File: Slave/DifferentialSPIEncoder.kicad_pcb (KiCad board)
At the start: 2 copper layers, 52.3 x 42.7 mm, 31 parts, among them J1 Debug, J2 8P8C_LED_Shielded, U2 AS5048A, U3 SN65HVD06D, U4 SN65HVD06D, U5 SN65HVD06D

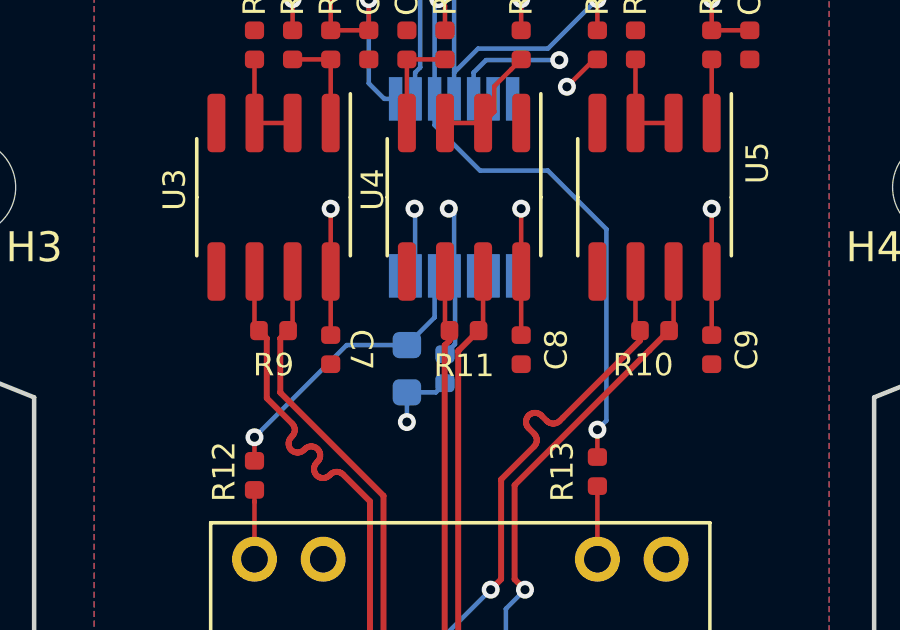
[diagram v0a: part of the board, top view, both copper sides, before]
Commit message: Swap AS5048A with AS5047U
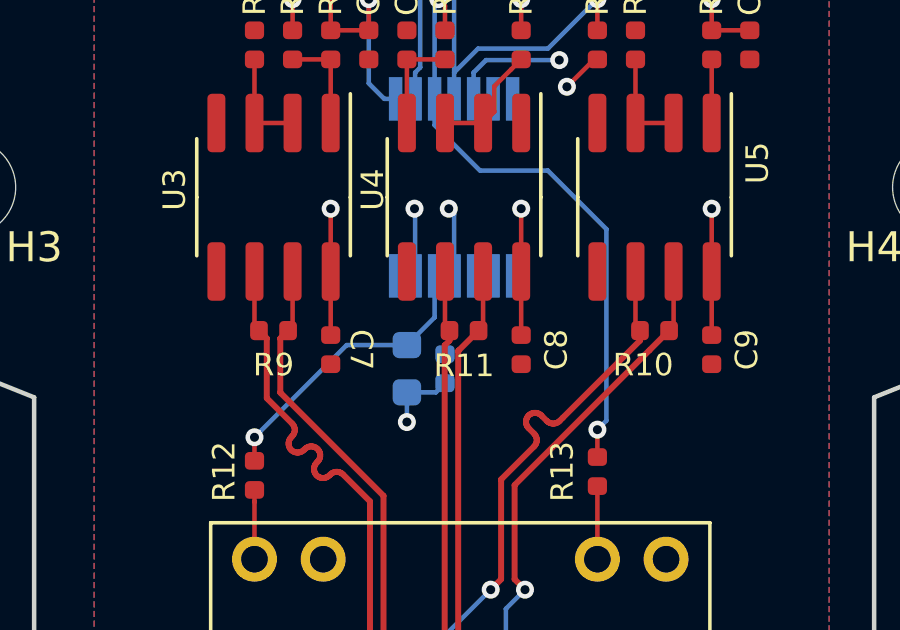
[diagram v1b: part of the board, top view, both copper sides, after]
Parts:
- removed C3: 100nF, Capacitor_SMD:C_0402_1005Metric
- removed U2: AS5048A, Package_SO:TSSOP-14_4.4x5mm_P0.65mm
- added C2: 1uF, Capacitor_SMD:C_0603_1608Metric, B.Cu at (98.4, 106.0)
- added U1: AS5047U, Package_SO:TSSOP-14_4.4x5mm_P0.65mm, B.Cu at (100.0, 100.0)
- C1: value 10uF -> 100nF; footprint Capacitor_SMD:C_0603_1608Metric -> Capacitor_SMD:C_0402_1005Metric
- moved C1 1.27 mm to (99.7, 106.0)
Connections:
- C1 pad 1: V3cap -> +5V
- R12 pad 2: V3cap -> +3V3
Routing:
- net V3cap: track 9.83 -> 0.00 mm, vias 1 -> 0
- net +3V3: track 0.00 -> 9.83 mm, vias 0 -> 1
- net +5V: track 21.2 -> 18.4 mm

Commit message: Update PCB
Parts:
- removed R1: 1k, Resistor_SMD:R_0402_1005Metric
- removed U5: SN65HVD06D, Package_SO:SOIC-8_3.9x4.9mm_P1.27mm
- added U2: MAX14783ExS, Package_SO:SOIC-8_3.9x4.9mm_P1.27mm, F.Cu at (94.0, 100.3)
- U3, U4: value SN65HVD06D -> MAX14783ExS
- moved U4 6.35 mm to (106.7, 100.3)
- moved U3 6.35 mm to (100.3, 100.3)
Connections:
- U3 pad 1: Net-(R2-Pad1) -> Net-(U3-Pad1)
- U3 pad 2: Net-(R7-Pad1) -> Net-(R8-Pad2)
- U3 pad 3: Net-(R7-Pad1) -> Net-(R8-Pad2)
- U3 pad 4: Net-(U3-Pad4) -> Net-(C6-Pad1)
- U3 pad 6: /CS_+ -> /MISO_+
- U3 pad 7: /CS_- -> /MISO_-
- U4 pad 1: Net-(U4-Pad1) -> Net-(R3-Pad1)
- U4 pad 2: Net-(R8-Pad2) -> Net-(R5-Pad1)
- U4 pad 3: Net-(R8-Pad2) -> Net-(R5-Pad1)
- U4 pad 4: Net-(C6-Pad1) -> Net-(U4-Pad4)
- U4 pad 6: /MISO_+ -> /CLK_+
- U4 pad 7: /MISO_- -> /CLK_-

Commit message: Fix Slave
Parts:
- removed J2: 8P8C_LED_Shielded, Connector_RJ:RJ45_Amphenol_RJHSE538X
- removed R12, R13: 220, Resistor_SMD:R_0402_1005Metric
- added C3: 1uF, Capacitor_SMD:C_0603_1608Metric_Pad1.05x0.95mm_HandSolder, F.Cu at (123.9, 79.5)
- added R1: 1k, Resistor_SMD:R_0603_1608Metric_Pad1.05x0.95mm_HandSolder, F.Cu at (115.2, 79.5)
- added U5: MA702, Package_DFN_QFN:QFN-16-1EP_3x3mm_P0.5mm_EP1.8x1.8mm, F.Cu at (107.2, 84.8)
- C1, C7, C8, C9: footprint Capacitor_SMD:C_0402_1005Metric -> Capacitor_SMD:C_0603_1608Metric_Pad1.05x0.95mm_HandSolder
- C2: footprint Capacitor_SMD:C_0603_1608Metric -> Capacitor_SMD:C_0603_1608Metric_Pad1.05x0.95mm_HandSolder
- C4, C5: value 2.2pF -> C; footprint Capacitor_SMD:C_0402_1005Metric -> Capacitor_SMD:C_0603_1608Metric_Pad1.05x0.95mm_HandSolder
- C6: value 2.2pF -> 22nF; footprint Capacitor_SMD:C_0402_1005Metric -> Capacitor_SMD:C_0603_1608Metric_Pad1.05x0.95mm_HandSolder
- J1: value Debug -> RJ45_Shielded; footprint Connector_PinHeader_2.54mm:PinHeader_2x03_P2.54mm_Vertical -> Connector_RJ:RJ45_Amphenol_RJHSE5380
- R10, R11, R2, R8: footprint Resistor_SMD:R_0402_1005Metric -> Resistor_SMD:R_0603_1608Metric_Pad1.05x0.95mm_HandSolder
- R3, R4: value 1k -> 10k; footprint Resistor_SMD:R_0402_1005Metric -> Resistor_SMD:R_0603_1608Metric_Pad1.05x0.95mm_HandSolder
- R5: value 10k -> 120; footprint Resistor_SMD:R_0402_1005Metric -> Resistor_SMD:R_0603_1608Metric_Pad1.05x0.95mm_HandSolder
- R6, R7: value 10k -> 1k; footprint Resistor_SMD:R_0402_1005Metric -> Resistor_SMD:R_0603_1608Metric_Pad1.05x0.95mm_HandSolder
- R9: value 120 -> 10k; footprint Resistor_SMD:R_0402_1005Metric -> Resistor_SMD:R_0603_1608Metric_Pad1.05x0.95mm_HandSolder
- U1: value AS5047U -> AS5048A
- moved R9 35.0 mm to (115.2, 77.0), turned to 0 degrees
- moved C9 32.3 mm to (123.9, 77.0), turned to 0 degrees
- moved C8 31.2 mm to (119.5, 79.5), turned to 0 degrees
- moved R2 23.1 mm to (116.3, 84.5), turned to 0 degrees
- moved R10 22.0 mm to (112.0, 83.4), turned to 0 degrees
- moved U4 21.5 mm to (108.8, 78.9), turned to 0 degrees
- moved R4 21.3 mm to (116.3, 82.0), turned to 0 degrees
- moved C5 20.7 mm to (119.5, 77.0), turned to 0 degrees
- moved C6 16.5 mm to (112.0, 85.9), turned to 0 degrees
- moved R8 16.3 mm to (116.3, 87.0), turned to 0 degrees
- moved R7 14.9 mm to (106.7, 88.7), turned to 0 degrees
- moved R11 13.1 mm to (107.4, 93.7), turned to 0 degrees
- moved J1 12.9 mm to (90.7, 84.7), turned to 0 degrees
- moved C7 12.8 mm to (103.0, 94.8), turned to 0 degrees
- moved R6 12.8 mm to (106.7, 91.2), turned to 0 degrees
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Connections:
- C4 pad 1: ~CSn -> /~CSn
- C5 pad 1: CLK -> /CLK
- J1 pad 1: MISO -> GNDD
- J1 pad 3: CLK -> /CLK-
- J1 pad 4: /MOSI -> /MISO-
- J1 pad 5: ~CSn -> /MISO+
- J1 pad 6: GND -> /CLK+
- R10 pad 1: /CLK_- -> /MISO+
- R10 pad 2: /CLK_+ -> /MISO-
- R11 pad 1: /MISO_- -> /CLK+
- R11 pad 2: /MISO_+ -> /CLK-
- R2 pad 2: ~CSn -> /~CSn
- R3 pad 1: Net-(R3-Pad1) -> Net-(R2-Pad1)
- R3 pad 2: CLK -> +5V
- R4 pad 1: MISO -> GND
- R4 pad 2: Net-(C6-Pad1) -> Net-(R4-Pad2)
- R5 pad 1: Net-(R5-Pad1) -> /CS+
- R5 pad 2: GND -> /CS-
- R6 pad 1: +5V -> /MISO
- R6 pad 2: Net-(R2-Pad1) -> Net-(C6-Pad1)
- R7 pad 2: GND -> /CLK
- R8 pad 1: +5V -> Net-(R8-Pad1)
- R8 pad 2: Net-(R8-Pad2) -> +5V
- R9 pad 1: /CS_- -> GND
- R9 pad 2: /CS_+ -> Net-(R9-Pad2)
- U1 pad 1: ~CSn -> (no net)
- U1 pad 10: Net-(U1-Pad10) -> (no net)
- U1 pad 14: /I -> (no net)
- U1 pad 2: CLK -> (no net)
- U1 pad 3: MISO -> (no net)
- U1 pad 4: /MOSI -> (no net)
- U1 pad 6: /B -> (no net)
- U1 pad 7: /A -> (no net)
- U1 pad 8: Net-(U1-Pad8) -> (no net)
- U1 pad 9: Net-(U1-Pad9) -> (no net)
- U2 pad 2: Net-(R7-Pad1) -> Net-(R4-Pad2)
- U2 pad 3: Net-(R7-Pad1) -> Net-(R4-Pad2)
- U2 pad 6: /CS_+ -> /CS+
- U2 pad 7: /CS_- -> /CS-
- U3 pad 2: Net-(R8-Pad2) -> Net-(R8-Pad1)
- U3 pad 3: Net-(R8-Pad2) -> Net-(R8-Pad1)
- U3 pad 6: /MISO_+ -> /MISO+
- U3 pad 7: /MISO_- -> /MISO-
- U4 pad 1: Net-(R3-Pad1) -> Net-(R7-Pad1)
- U4 pad 2: Net-(R5-Pad1) -> Net-(R9-Pad2)
- U4 pad 3: Net-(R5-Pad1) -> Net-(R9-Pad2)
- U4 pad 6: /CLK_+ -> /CLK+
- U4 pad 7: /CLK_- -> /CLK-
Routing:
- net /CLK-: track 0.00 -> 41.1 mm, vias 0 -> 1
- net MISO: track 27.6 -> 0.00 mm, vias 2 -> 0
- net +5V: track 18.4 -> 43.6 mm
- net CLK: track 24.8 -> 0.00 mm, vias 1 -> 0
- net Net-(R8-Pad1): track 0.00 -> 19.4 mm, vias 0 -> 1
- net Net-(R4-Pad2): track 0.00 -> 18.8 mm, vias 0 -> 1
- net /CLK_+: track 18.8 -> 0.00 mm, vias 1 -> 0
- net Net-(R1-Pad2): track 0.00 -> 18.8 mm, vias 0 -> 1
- net /CLK_-: track 18.8 -> 0.00 mm, vias 1 -> 0
- net Net-(J2-PadSH): track 17.8 -> 0.00 mm
- net /MISO: track 0.00 -> 17.8 mm
- net /MISO+: track 0.00 -> 17.8 mm
- net /CS_+: track 17.8 -> 0.00 mm
- net /CS_-: track 17.8 -> 0.00 mm
- net /CS-: track 0.00 -> 17.8 mm
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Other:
- net class Default removed

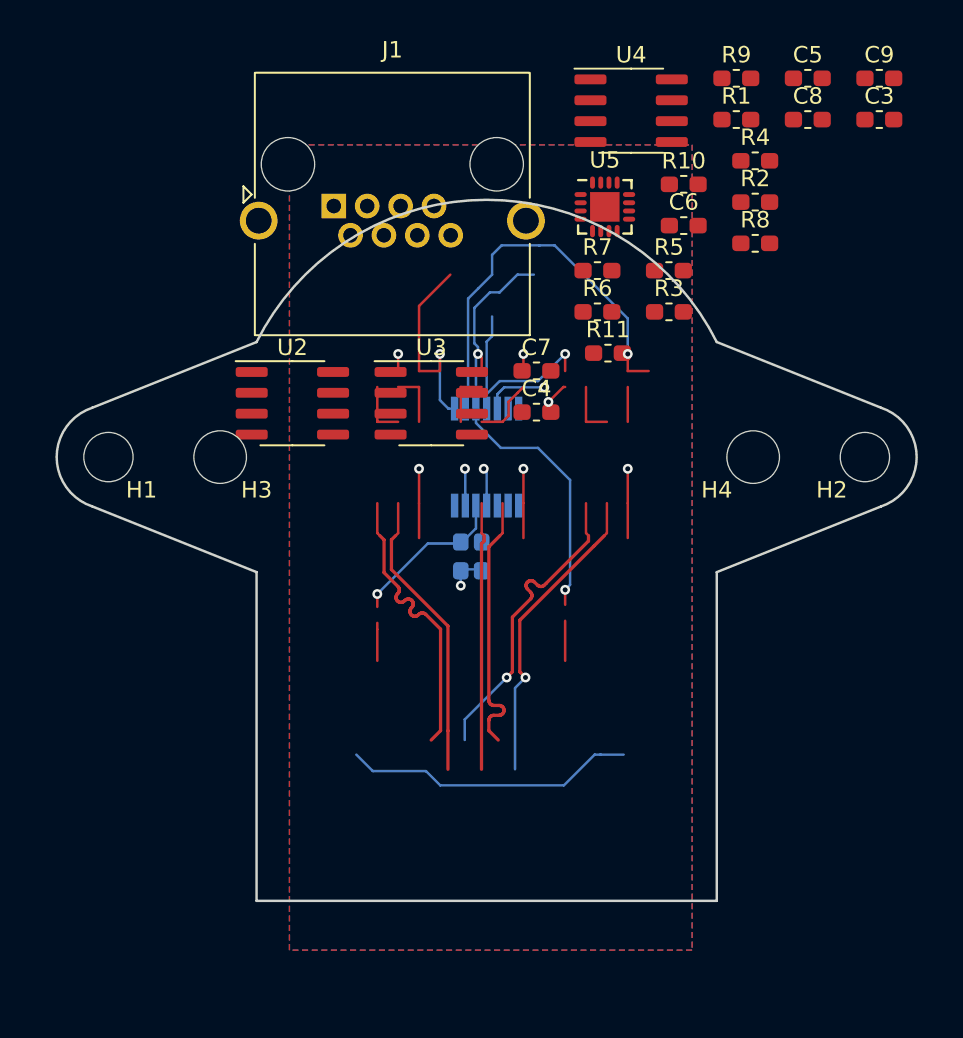
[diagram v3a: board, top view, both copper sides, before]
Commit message: Revert slave pcb to older build of Kicad
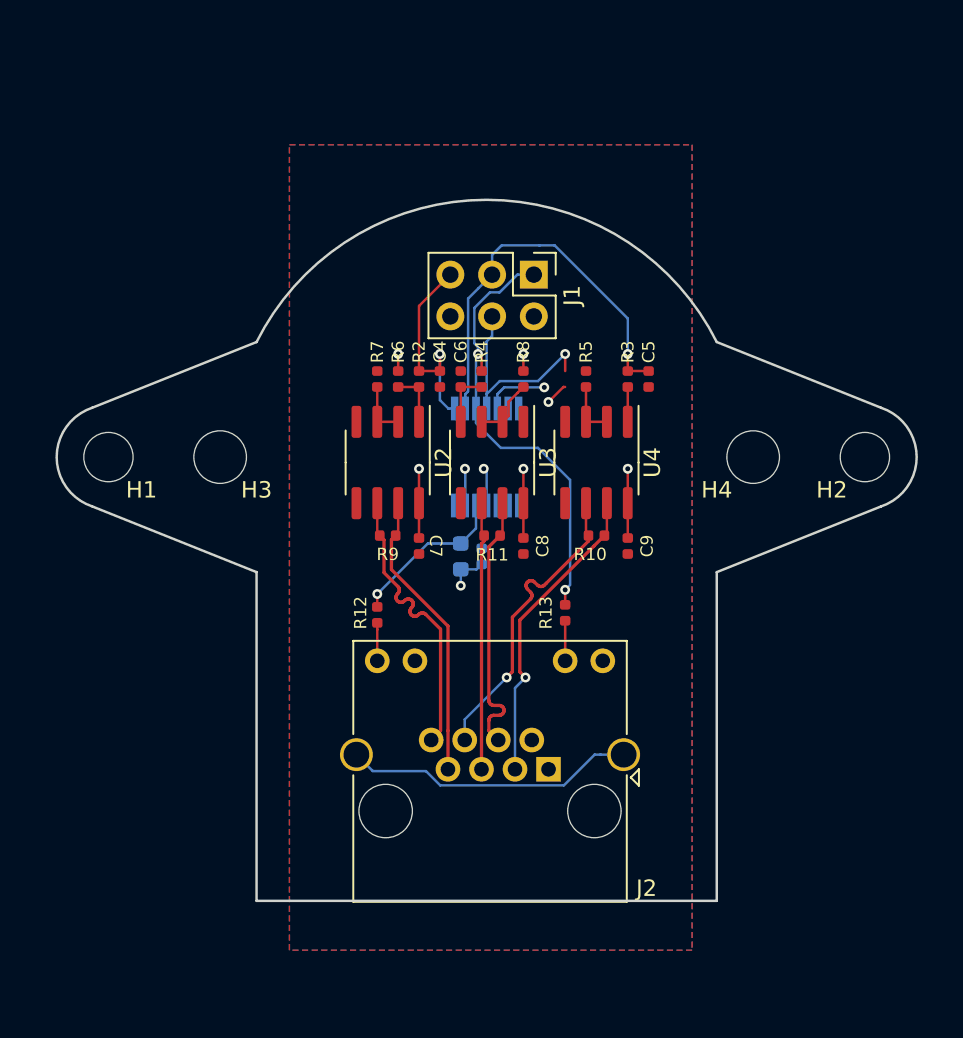
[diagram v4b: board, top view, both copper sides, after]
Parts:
- removed C3: 1uF, Capacitor_SMD:C_0603_1608Metric_Pad1.05x0.95mm_HandSolder
- removed R1: 1k, Resistor_SMD:R_0603_1608Metric_Pad1.05x0.95mm_HandSolder
- removed U5: MA702, Package_DFN_QFN:QFN-16-1EP_3x3mm_P0.5mm_EP1.8x1.8mm
- added J2: 8P8C_LED_Shielded, Connector_RJ:RJ45_Amphenol_RJHSE538X, F.Cu at (103.8, 119.0)
- added R12: 220, Resistor_SMD:R_0402_1005Metric, F.Cu at (93.3, 109.6)
- added R13: 220, Resistor_SMD:R_0402_1005Metric, F.Cu at (104.8, 109.5)
- C1, C7, C8, C9: footprint Capacitor_SMD:C_0603_1608Metric_Pad1.05x0.95mm_HandSolder -> Capacitor_SMD:C_0402_1005Metric
- C2: footprint Capacitor_SMD:C_0603_1608Metric_Pad1.05x0.95mm_HandSolder -> Capacitor_SMD:C_0603_1608Metric
- C4, C5: value C -> 2.2pF; footprint Capacitor_SMD:C_0603_1608Metric_Pad1.05x0.95mm_HandSolder -> Capacitor_SMD:C_0402_1005Metric
- C6: value 22nF -> 2.2pF; footprint Capacitor_SMD:C_0603_1608Metric_Pad1.05x0.95mm_HandSolder -> Capacitor_SMD:C_0402_1005Metric
- J1: value RJ45_Shielded -> Debug; footprint Connector_RJ:RJ45_Amphenol_RJHSE5380 -> Connector_PinHeader_2.54mm:PinHeader_2x03_P2.54mm_Vertical
- R10, R11, R2, R8: footprint Resistor_SMD:R_0603_1608Metric_Pad1.05x0.95mm_HandSolder -> Resistor_SMD:R_0402_1005Metric
- R3, R4: value 10k -> 1k; footprint Resistor_SMD:R_0603_1608Metric_Pad1.05x0.95mm_HandSolder -> Resistor_SMD:R_0402_1005Metric
- R5: value 120 -> 10k; footprint Resistor_SMD:R_0603_1608Metric_Pad1.05x0.95mm_HandSolder -> Resistor_SMD:R_0402_1005Metric
- R6, R7: value 1k -> 10k; footprint Resistor_SMD:R_0603_1608Metric_Pad1.05x0.95mm_HandSolder -> Resistor_SMD:R_0402_1005Metric
- R9: value 10k -> 120; footprint Resistor_SMD:R_0603_1608Metric_Pad1.05x0.95mm_HandSolder -> Resistor_SMD:R_0402_1005Metric
- U1: value AS5048A -> AS5047U
- moved R9 35.0 mm to (94.0, 104.8), turned to 180 degrees
- moved C9 32.3 mm to (108.6, 105.4), turned to -90 degrees
- moved C8 31.2 mm to (102.2, 105.4), turned to -90 degrees
- moved R2 23.1 mm to (95.9, 95.2), turned to 90 degrees
- moved R10 22.0 mm to (106.7, 104.8), turned to 180 degrees
- moved U4 21.5 mm to (106.7, 100.3), turned to -90 degrees
- moved R4 21.3 mm to (99.7, 95.2), turned to -90 degrees
- moved C5 20.7 mm to (109.9, 95.2), turned to -90 degrees
- moved C6 16.5 mm to (98.4, 95.2), turned to 90 degrees
- moved R8 16.3 mm to (102.2, 95.2), turned to -90 degrees
- moved R7 14.9 mm to (93.3, 95.2), turned to 90 degrees
- moved R11 13.1 mm to (100.3, 104.8), turned to 180 degrees
- moved J1 12.9 mm to (102.9, 88.9), turned to -90 degrees
- moved C7 12.8 mm to (95.9, 105.4), turned to -90 degrees
- moved R6 12.8 mm to (94.6, 95.2), turned to -90 degrees
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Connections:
- C4 pad 1: /~CSn -> ~CSn
- C5 pad 1: /CLK -> CLK
- J1 pad 1: GNDD -> MISO
- J1 pad 3: /CLK- -> CLK
- J1 pad 4: /MISO- -> /MOSI
- J1 pad 5: /MISO+ -> ~CSn
- J1 pad 6: /CLK+ -> GND
- R10 pad 1: /MISO+ -> /CLK_-
- R10 pad 2: /MISO- -> /CLK_+
- R11 pad 1: /CLK+ -> /MISO_-
- R11 pad 2: /CLK- -> /MISO_+
- R2 pad 2: /~CSn -> ~CSn
- R3 pad 1: Net-(R2-Pad1) -> Net-(R3-Pad1)
- R3 pad 2: +5V -> CLK
- R4 pad 1: GND -> MISO
- R4 pad 2: Net-(R4-Pad2) -> Net-(C6-Pad1)
- R5 pad 1: /CS+ -> Net-(R5-Pad1)
- R5 pad 2: /CS- -> GND
- R6 pad 1: /MISO -> +5V
- R6 pad 2: Net-(C6-Pad1) -> Net-(R2-Pad1)
- R7 pad 2: /CLK -> GND
- R8 pad 1: Net-(R8-Pad1) -> +5V
- R8 pad 2: +5V -> Net-(R8-Pad2)
- R9 pad 1: GND -> /CS_-
- R9 pad 2: Net-(R9-Pad2) -> /CS_+
- U1 pad 1: (no net) -> ~CSn
- U1 pad 10: (no net) -> Net-(U1-Pad10)
- U1 pad 14: (no net) -> /I
- U1 pad 2: (no net) -> CLK
- U1 pad 3: (no net) -> MISO
- U1 pad 4: (no net) -> /MOSI
- U1 pad 6: (no net) -> /B
- U1 pad 7: (no net) -> /A
- U1 pad 8: (no net) -> Net-(U1-Pad8)
- U1 pad 9: (no net) -> Net-(U1-Pad9)
- U2 pad 2: Net-(R4-Pad2) -> Net-(R7-Pad1)
- U2 pad 3: Net-(R4-Pad2) -> Net-(R7-Pad1)
- U2 pad 6: /CS+ -> /CS_+
- U2 pad 7: /CS- -> /CS_-
- U3 pad 2: Net-(R8-Pad1) -> Net-(R8-Pad2)
- U3 pad 3: Net-(R8-Pad1) -> Net-(R8-Pad2)
- U3 pad 6: /MISO+ -> /MISO_+
- U3 pad 7: /MISO- -> /MISO_-
- U4 pad 1: Net-(R7-Pad1) -> Net-(R3-Pad1)
- U4 pad 2: Net-(R9-Pad2) -> Net-(R5-Pad1)
- U4 pad 3: Net-(R9-Pad2) -> Net-(R5-Pad1)
- U4 pad 6: /CLK+ -> /CLK_+
- U4 pad 7: /CLK- -> /CLK_-
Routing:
- net /CLK-: track 41.1 -> 0.00 mm, vias 1 -> 0
- net MISO: track 0.00 -> 27.6 mm, vias 0 -> 2
- net +5V: track 43.6 -> 18.4 mm
- net CLK: track 0.00 -> 24.8 mm, vias 0 -> 1
- net Net-(R8-Pad1): track 19.4 -> 0.00 mm, vias 1 -> 0
- net Net-(R4-Pad2): track 18.8 -> 0.00 mm, vias 1 -> 0
- net /CLK_+: track 0.00 -> 18.8 mm, vias 0 -> 1
- net Net-(R1-Pad2): track 18.8 -> 0.00 mm, vias 1 -> 0
- net /CLK_-: track 0.00 -> 18.8 mm, vias 0 -> 1
- net Net-(J2-PadSH): track 0.00 -> 17.8 mm
- net /MISO: track 17.8 -> 0.00 mm
- net /MISO+: track 17.8 -> 0.00 mm
- net /CS_+: track 0.00 -> 17.8 mm
- net /CS_-: track 0.00 -> 17.8 mm
- net /CS-: track 17.8 -> 0.00 mm
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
